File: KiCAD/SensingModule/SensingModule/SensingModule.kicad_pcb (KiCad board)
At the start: 2 copper layers, 90 x 70 mm, 11 parts

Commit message: 基板の中に納めました
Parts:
- added C1: 10uF, Capacitor_SMD:C_1206_3216Metric_Pad1.33x1.80mm_HandSolder, F.Cu at (187.3, 85.7)
- added C2: 2.2uF, Capacitor_SMD:C_0603_1608Metric_Pad1.08x0.95mm_HandSolder, F.Cu at (182.1, 85.2)
- added C3: 0.1uF, Capacitor_SMD:C_0603_1608Metric_Pad1.08x0.95mm_HandSolder, F.Cu at (182.1, 87.8)
- added C4: 0.1uF, Capacitor_SMD:C_0603_1608Metric_Pad1.08x0.95mm_HandSolder, F.Cu at (168.3, 95.5)
- added C5: 0.1uF, Capacitor_SMD:C_0603_1608Metric_Pad1.08x0.95mm_HandSolder, F.Cu at (168.3, 98.0)
- added C6: 0.1uF, Capacitor_SMD:C_0603_1608Metric_Pad1.08x0.95mm_HandSolder, F.Cu at (168.3, 100.5)
- added C7: 15pF, Capacitor_SMD:C_0603_1608Metric_Pad1.08x0.95mm_HandSolder, F.Cu at (173.1, 91.3)
- added C8: 15pF, Capacitor_SMD:C_0603_1608Metric_Pad1.08x0.95mm_HandSolder, F.Cu at (173.1, 93.8)
- added D3: R, LED_SMD:LED_0603_1608Metric_Pad1.05x0.95mm_HandSolder, F.Cu at (192.5, 85.3)
- added D4: GS1010FL, Diode_SMD:D_SOD-123F, F.Cu at (187.1, 89.0)
- added D5: B, LED_SMD:LED_0603_1608Metric_Pad1.05x0.95mm_HandSolder, F.Cu at (177.7, 91.8)
- added D6: B, LED_SMD:LED_0603_1608Metric_Pad1.05x0.95mm_HandSolder, F.Cu at (177.7, 94.4)
- added R10: 2.4kR, Resistor_SMD:R_0603_1608Metric_Pad0.98x0.95mm_HandSolder, F.Cu at (182.1, 90.3)
- added R11: 120R, Resistor_SMD:R_0603_1608Metric_Pad0.98x0.95mm_HandSolder, F.Cu at (173.1, 96.3)
- added R12: 680R, Resistor_SMD:R_0603_1608Metric_Pad0.98x0.95mm_HandSolder, F.Cu at (173.1, 98.8)
- added R13: 680R, Resistor_SMD:R_0603_1608Metric_Pad0.98x0.95mm_HandSolder, F.Cu at (173.1, 101.3)
- added R14: 10kR, Resistor_SMD:R_0603_1608Metric_Pad0.98x0.95mm_HandSolder, F.Cu at (173.1, 103.8)
- added R15: 10kR, Resistor_SMD:R_0603_1608Metric_Pad0.98x0.95mm_HandSolder, F.Cu at (168.3, 92.7)
- added U1: Arduino MKR WAN 1310, ARDUINO_MKR_WAN_1310:BOARD_ARDUINO_MKR_WAN_1310, F.Cu at (152.5, 86.1)
- added U2: NJM7805SDL1, Package_TO_SOT_SMD:TO-252-2, F.Cu at (186.3, 70.2)
- added U3: MCP2562-E-P, Package_DIP:DIP-8_W7.62mm, F.Cu at (129.2, 95.3)
- added U4: MCP2515-I/P, Package_DIP:DIP-18_W7.62mm, F.Cu at (170.2, 66.2)
- added U5: MB85RS2MT, Package_DIP:DIP-8_W7.62mm, F.Cu at (116.6, 80.0)
- added U6: MB85RS2MT, Package_DIP:DIP-8_W7.62mm, F.Cu at (129.2, 80.3)
- added U7: MB85RS2MT, Package_DIP:DIP-8_W7.62mm, F.Cu at (116.3, 66.1)
- added U8: MB85RS2MT, Package_DIP:DIP-8_W7.62mm, F.Cu at (129.4, 65.8)
- added Y1: 8MHz, Crystal:Crystal_SMD_HC49-SD, F.Cu at (187.0, 78.5)
- moved D2 110.5 mm to (123.3, 96.3)
- moved D1 110.5 mm to (123.4, 93.4)
- moved R2 110.2 mm to (118.8, 95.7)
- moved R1 109.9 mm to (118.8, 92.7)
- moved R5 107.9 mm to (119.0, 99.0)
- moved R7 106.6 mm to (119.1, 101.5)
- moved R9 105.7 mm to (119.2, 104.6)
- moved R4 104.1 mm to (115.0, 95.6)
- moved R3 104.0 mm to (114.9, 93.0)
- moved R6 103.2 mm to (115.0, 99.0)
- moved R8 102.2 mm to (114.8, 102.5)

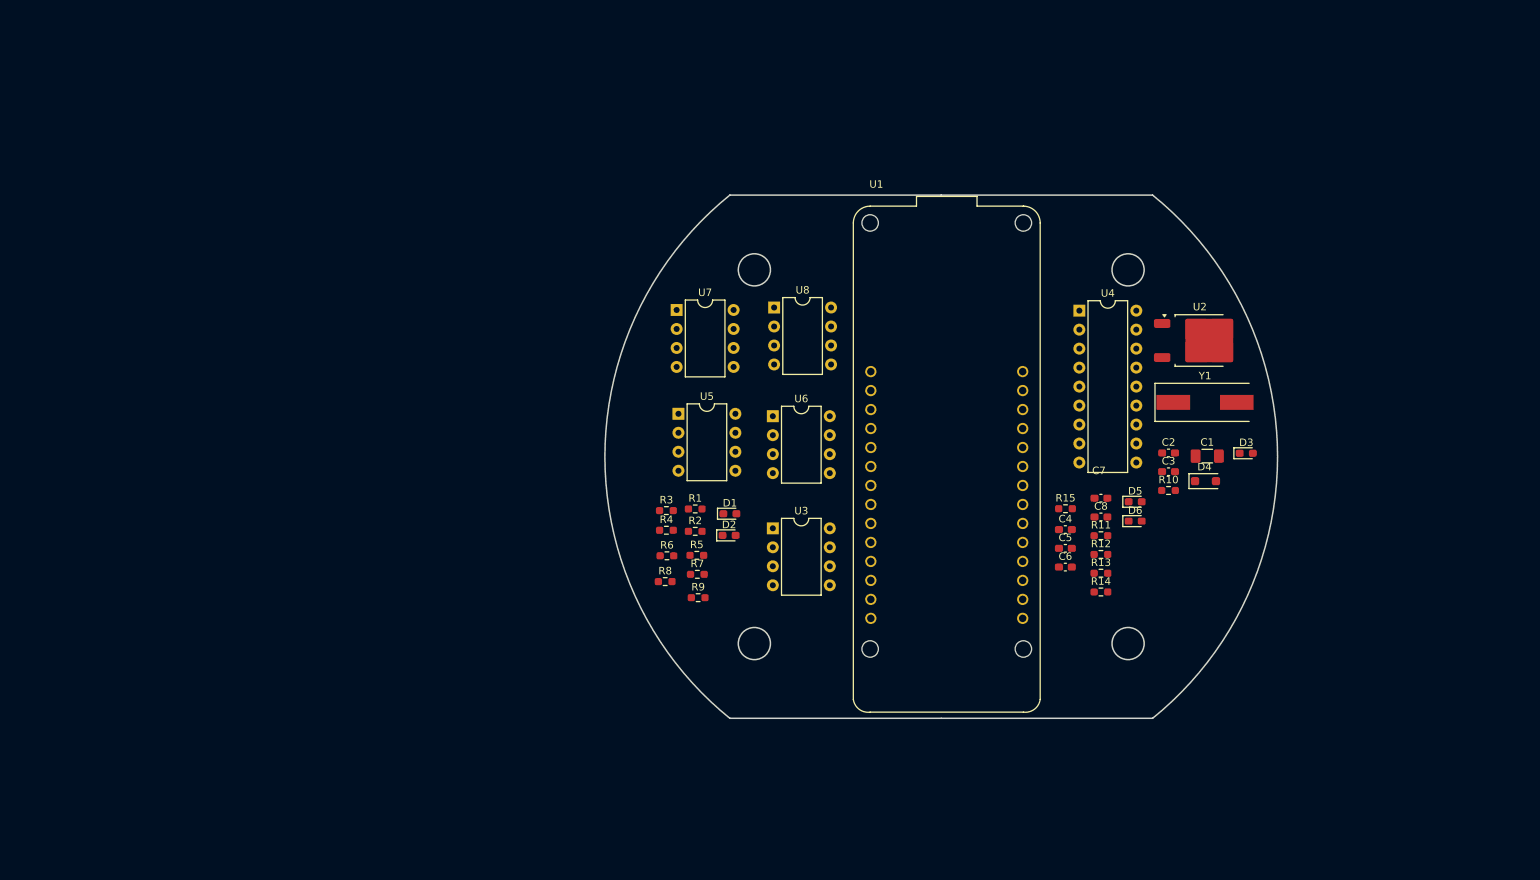
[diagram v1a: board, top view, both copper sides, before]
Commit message: 基板とmkrの位置を中原さんのものに合わせました
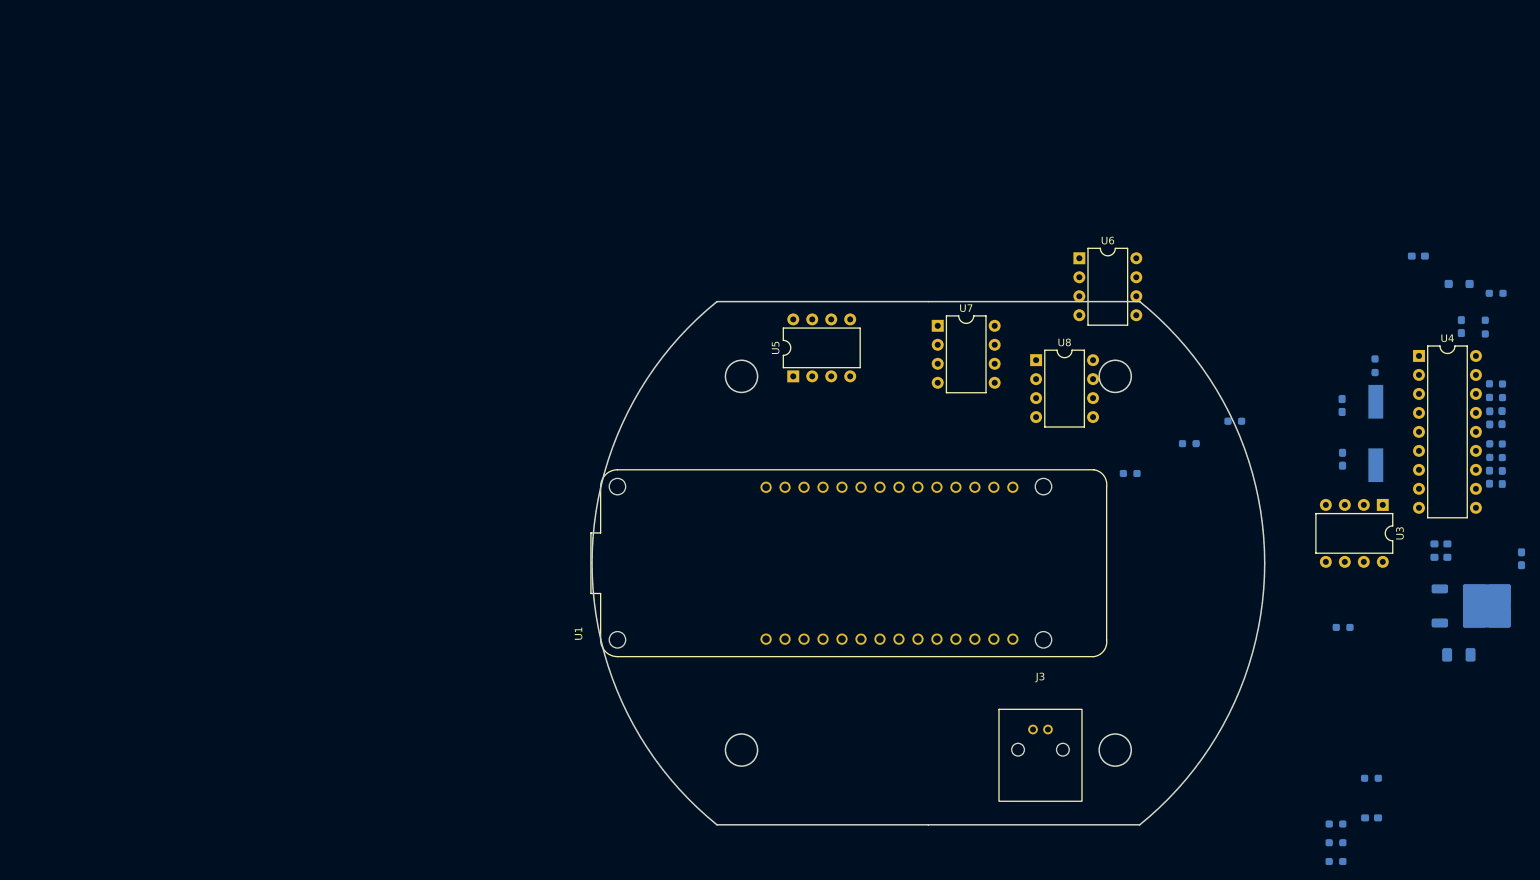
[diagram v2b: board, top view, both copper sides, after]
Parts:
- added J3: TERMISTOR, TSRP_Connector_Hirose:DF51-2P-2DS, F.Cu at (165.0, 131.7)
- C1, C2, C3, C4, C5, C6, C7, C8, D1, D2, D3, D4, D5, D6, R1, R10, R11, R12, R13, R14, R15, R2, R3, R4, R5, R6, R7, R8, R9, U2, Y1: moved to B.Cu
- moved R8 111.7 mm to (225.1, 84.9), turned to -90 degrees
- moved R9 111.4 mm to (224.5, 68.4), turned to 90 degrees
- moved R1 109.2 mm to (226.8, 76.9), turned to -90 degrees
- moved R7 109.0 mm to (226.8, 85.0), turned to -90 degrees
- moved R2 107.9 mm to (225.1, 76.9), turned to -90 degrees
- moved D1 104.1 mm to (226.8, 80.5), turned to 90 degrees
- moved D2 103.0 mm to (225.1, 80.6), turned to 90 degrees
- moved R6 91.0 mm to (205.5, 108.6)
- moved U3 81.7 mm to (210.8, 92.2), turned to -90 degrees
- moved R4 77.4 mm to (191.0, 81.0), turned to 180 degrees
- moved R3 70.5 mm to (184.9, 84.0), turned to 180 degrees
- moved C6 62.0 mm to (221.3, 68.3), turned to 90 degrees
- moved C4 61.2 mm to (229.4, 99.4), turned to -90 degrees
- moved R5 59.0 mm to (177.0, 88.0), turned to 180 degrees
- moved C5 54.6 mm to (209.3, 134.1), turned to 180 degrees
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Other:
- outline, holes or cut-outs redrawn
- board text added: "bme280"
- board text added: "bno055"

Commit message: コネクタ以外は基板の中に入った
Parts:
- moved U2 106.6 mm to (116.9, 102.8)
- moved Y1 92.9 mm to (117.6, 93.1), turned to 0 degrees
- moved D1 87.1 mm to (141.6, 99.1)
- moved D2 87.1 mm to (140.0, 99.1)
- moved D5 87.1 mm to (141.7, 107.1)
- moved R1 87.1 mm to (141.7, 95.5)
- moved R7 87.1 mm to (141.7, 103.5)
- moved R8 87.1 mm to (140.0, 103.5)
- moved D6 87.1 mm to (140.0, 107.1)
- moved R2 87.1 mm to (140.0, 95.5)
- moved R13 85.0 mm to (128.3, 100.0)
- moved R12 85.0 mm to (128.3, 97.5)
- moved R14 85.0 mm to (128.3, 102.5)
- moved R10 81.7 mm to (154.5, 103.6)
- moved D3 79.6 mm to (149.9, 103.8)
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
